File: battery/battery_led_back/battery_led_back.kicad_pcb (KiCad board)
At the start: 2 copper layers, 14 parts

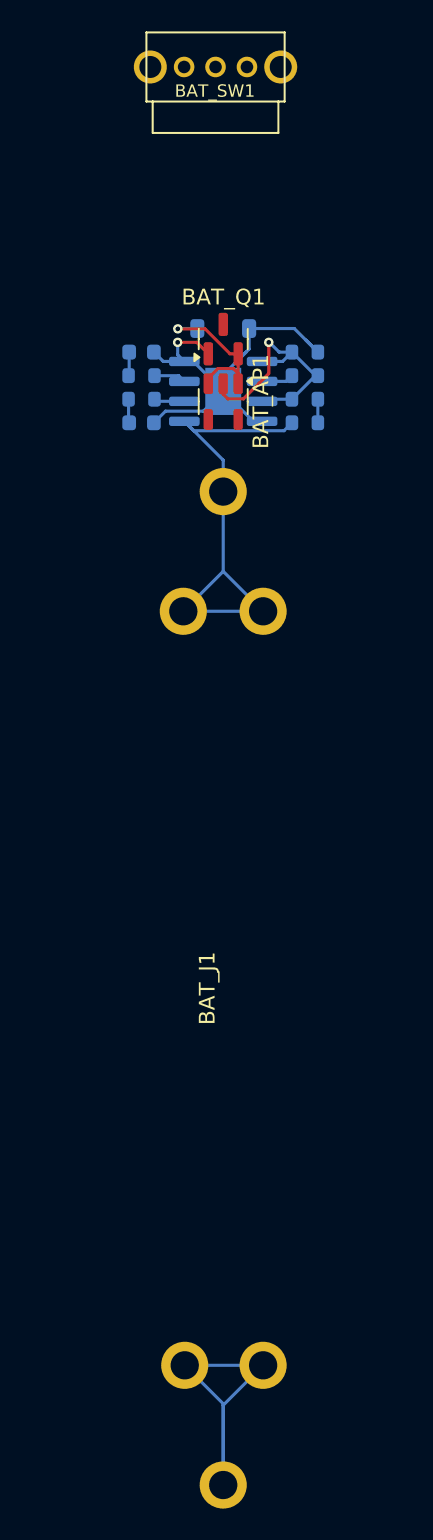
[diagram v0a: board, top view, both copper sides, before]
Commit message: use SY8088AAC in battery modules
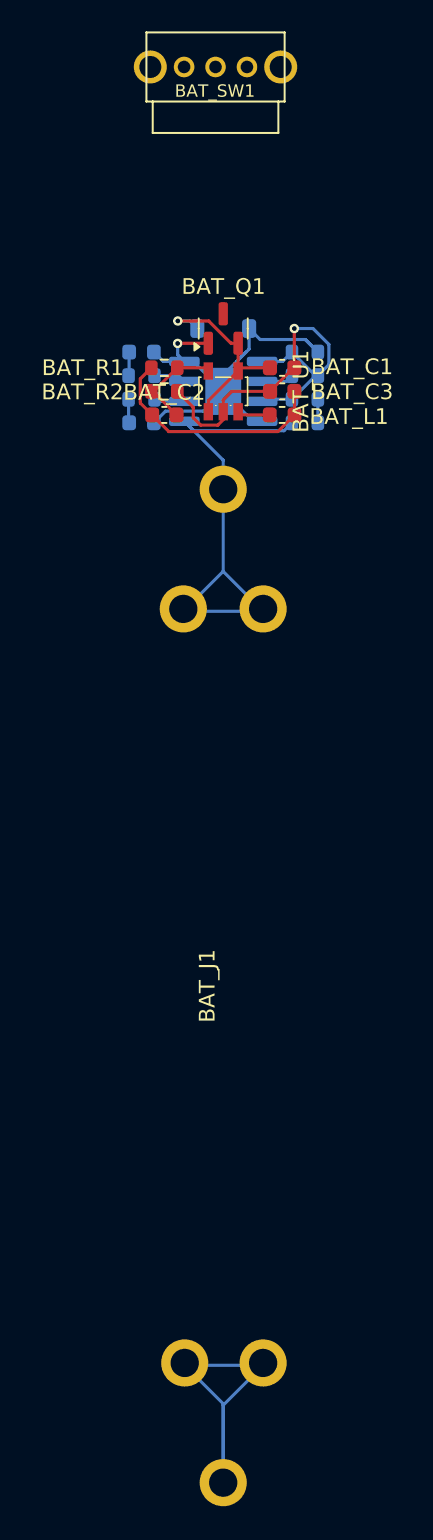
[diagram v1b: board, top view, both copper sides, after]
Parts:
- removed BAT_AP1: AP2112K-3.3, ErgoCai.pretty:SOT-23-5
- added BAT_C1: 22uF, ErgoCai.pretty:C_0603_1608Metric, F.Cu at (3.75, -39.5)
- added BAT_C2: 10uF, ErgoCai.pretty:C_0603_1608Metric, F.Cu at (-3.75, -36.5)
- added BAT_C3: 22uF, ErgoCai.pretty:C_0603_1608Metric, F.Cu at (3.75, -38.0)
- added BAT_L1: 2.2µH, ErgoCai.pretty:L_0603_1608Metric, F.Cu at (3.75, -36.5)
- added BAT_R1: 450K, ErgoCai.pretty:R_0603_1608Metric, F.Cu at (-3.75, -39.5)
- added BAT_R2: 100K, ErgoCai.pretty:R_0603_1608Metric, F.Cu at (-3.75, -38.0)
- added BAT_U1: SY8088AAC, ErgoCai.pretty:SOT-23-5_L3.0-W1.7-P0.95-LS2.8-BR, F.Cu at (0.00, -38.0)
- moved BAT_Q1 0.67 mm to (0.00, -42.0)
- moved BAT_J1 0.15 mm to (0.00, -0.15)
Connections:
- net Net-(BAT_AP1-EN) renamed VIN
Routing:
- net VCC: track 0.00 -> 15.0 mm
- net GND: track 38.9 -> 49.2 mm
- net Net-(BAT_U1-FB): track 0.00 -> 6.62 mm
- net VIN: track 10.9 -> 13.1 mm
- net Net-(BAT_U1-LX): track 0.00 -> 2.10 mm

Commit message: update battery_led_back.kicad_pcb
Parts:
- moved BAT_R1 2.97 mm to (-3.75, -36.5)
- moved BAT_C2 1.51 mm to (-3.75, -38.0)
- moved BAT_R2 1.50 mm to (-3.75, -39.5), turned to 180 degrees
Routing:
- net GND: track 49.2 -> 52.8 mm
- net VCC: track 15.0 -> 13.4 mm
- net Net-(BAT_U1-FB): track 6.62 -> 5.17 mm
- net VBAT: track 30.2 -> 31.1 mm

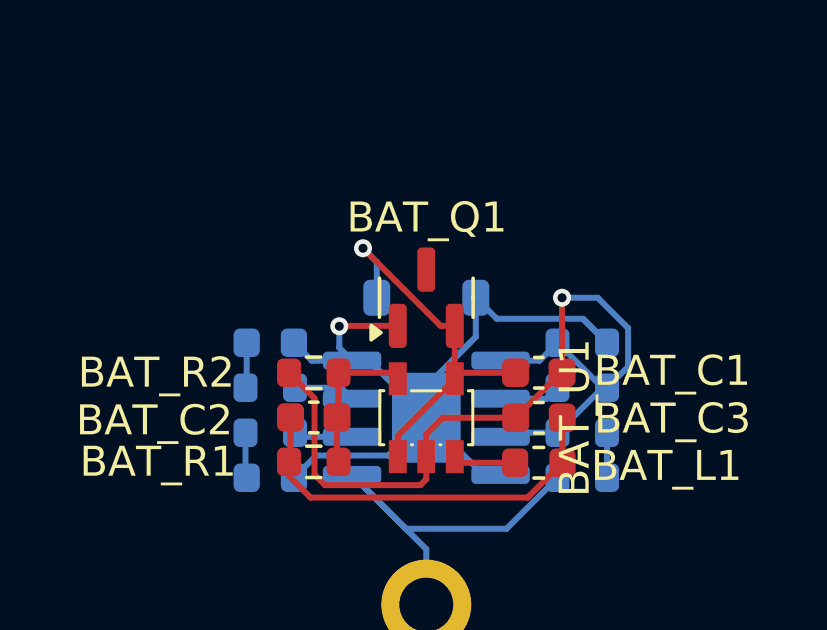
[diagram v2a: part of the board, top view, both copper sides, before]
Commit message: update battery_led_back.kicad_pcb
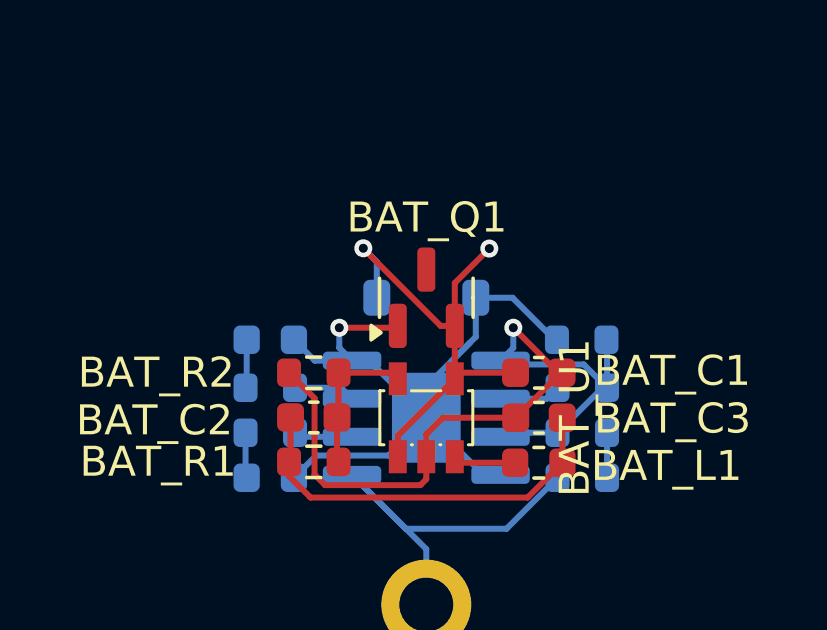
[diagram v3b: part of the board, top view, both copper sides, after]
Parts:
- moved BAT_R_G1 0.10 mm to (5.18, -40.6), turned to 0 degrees
- moved BAT_LEDR1 0.10 mm to (-5.20, -40.6)
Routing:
- net VIN: track 13.2 -> 16.3 mm, vias 1 -> 2
- net GND: track 52.8 -> 50.0 mm
- net VBUS: track 28.9 -> 26.2 mm

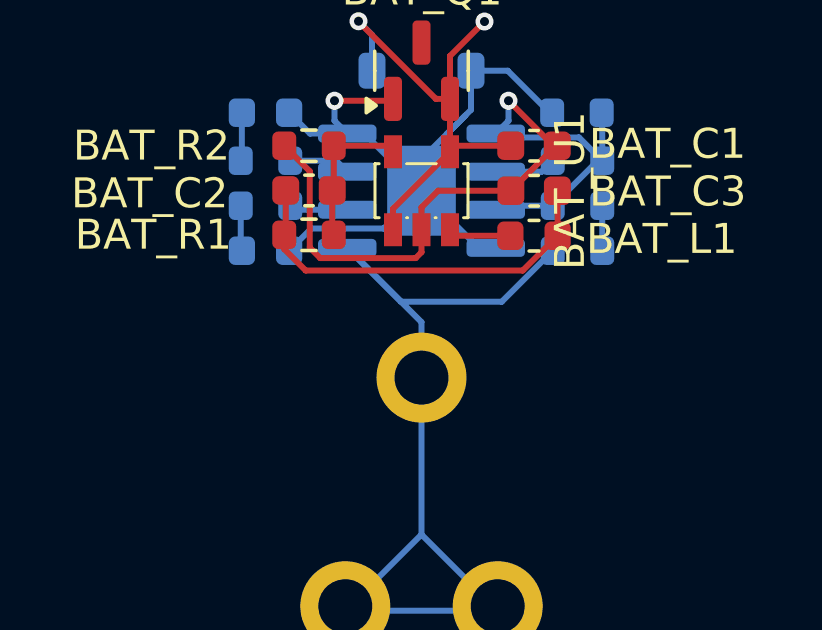
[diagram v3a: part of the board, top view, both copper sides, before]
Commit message: update bat line
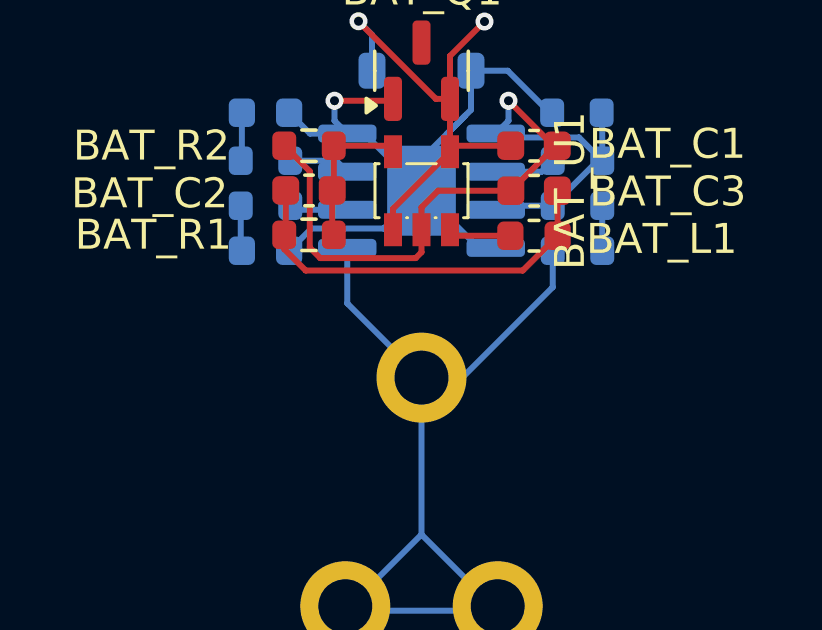
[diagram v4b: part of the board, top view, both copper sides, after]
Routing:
- net VBAT: track 31.1 -> 29.5 mm
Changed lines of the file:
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@@
 	)
 	(segment
-		(start 0 -33.62)
-		(end 0 -31.62)
+		(start 0 -31.77)
+		(end -2.475 -34.245)
+		(width 0.2)
+		(layer "B.Cu")
+		(net 1)
+	)
+	(segment
+		(start -2.475 -34.245)
+		(end -2.475 -36.095)
 		(width 0.2)
 		(layer "B.Cu")
@@
 	)
 	(segment
-		(start -2.475 -36.095)
-		(end 0 -33.62)
+		(start 4.375 -34.785)
+		(end 1.36 -31.77)
 		(width 0.2)
 		(layer "B.Cu")
@@
 	)
 	(segment
-		(start 4.375 -36)
-		(end 2.675 -34.3)
+		(start 1.36 -31.77)
+		(end 0 -31.77)
 		(width 0.2)
 		(layer "B.Cu")
@@
 	)
 	(segment
-		(start 2.675 -34.3)
-		(end -0.68 -34.3)
-		(width 0.2)
-		(layer "B.Cu")
-		(net 1)
-	)
-	(segment
 		(start 0 -26.54)
 		(end 0 -31.62)
@@
 	)
 	(segment
-		(start -0.68 -34.3)
-		(end -2.475 -36.095)
+		(start 4.375 -36)
+		(end 4.375 -34.785)
 		(width 0.2)
 		(layer "B.Cu")
